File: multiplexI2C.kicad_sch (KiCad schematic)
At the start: 26 parts, among them J17 Conn_01x04_Pin, J18 PinSocket_1x20_P2.54mm_Vertic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, J19 PinSocket_1x20_P2.54mm_Vertic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, J20 Screw_Terminal_01x02, J9 header_0.25sqmm_1x04_P4.2mm_D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, U1 TCA9548A

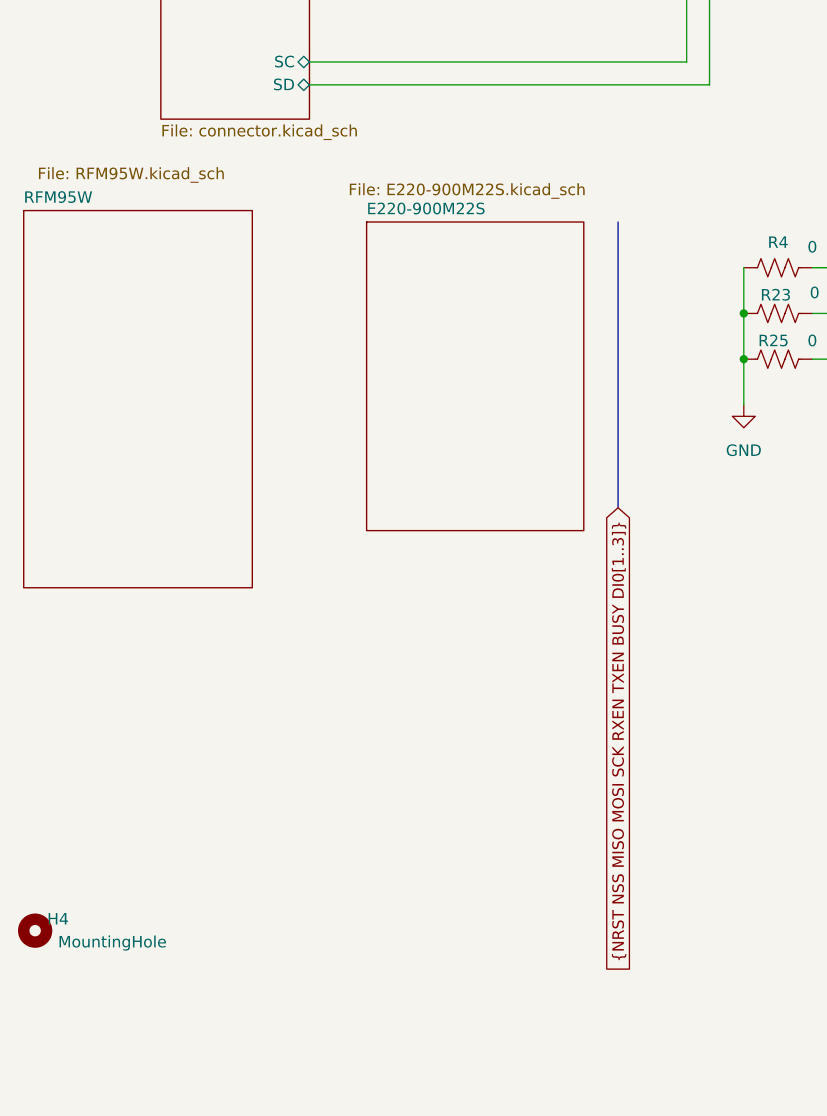
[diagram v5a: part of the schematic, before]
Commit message: DRC ot errors. 3D not showing U2.
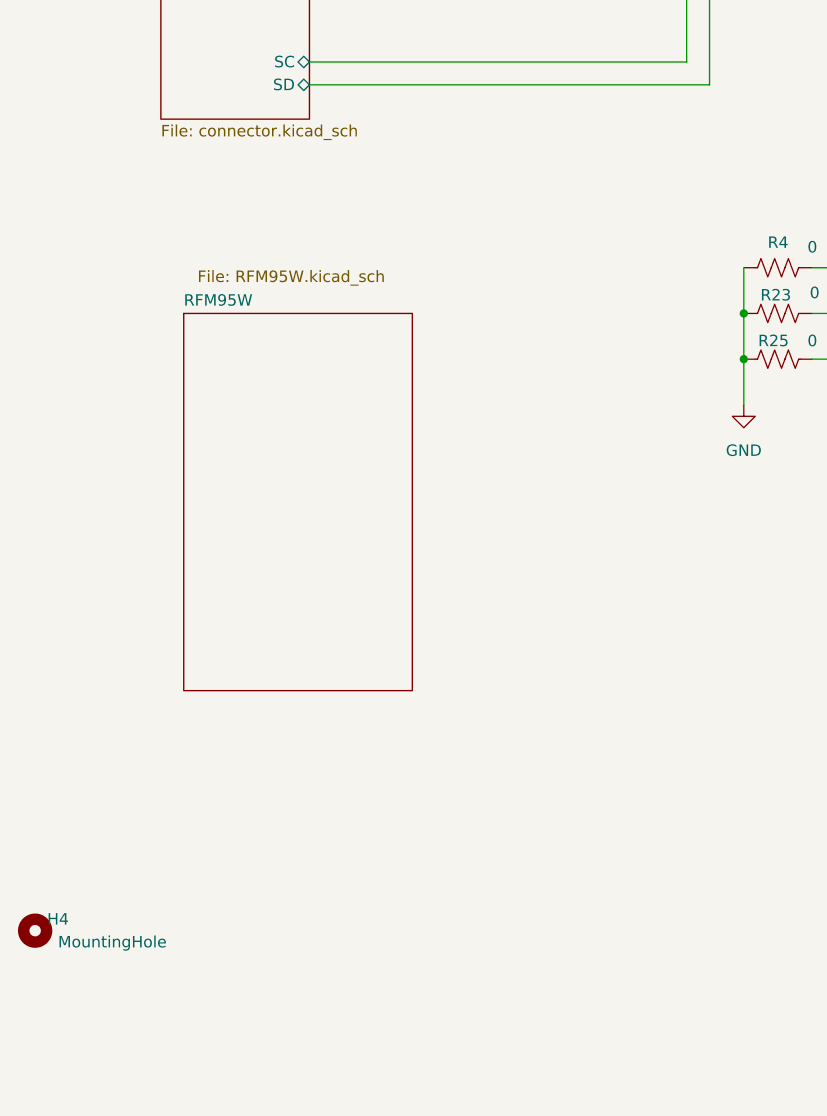
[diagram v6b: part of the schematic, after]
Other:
- removed sheet E220-900M22S
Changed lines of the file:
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@@
 		)
 	)
-	(bus
-		(pts
-			(xy 83.82 181.61) (xy 83.82 213.36)
-		)
-		(stroke
-			(width 0)
-			(type default)
-		)
-	)
 	(wire
 		(pts
@@
 		)
 	)
-	(global_label "{NRST NSS MISO MOSI SCK RXEN TXEN BUSY DI0[1..3]}"
-		(shape input)
-		(at 83.82 213.36 270)
-		(fields_autoplaced yes)
-		(effects
-			(font
-				(size 1.27 1.27)
-			)
-			(justify right)
-		)
-		(property "Intersheetrefs" "${INTERSHEET_REFS}"
-			(at 83.82 270.1689 90)
-			(effects
-				(font
-					(size 1.27 1.27)
-				)
-				(justify right)
-				(hide yes)
-			)
-		)
-	)
 	(global_label "{RESET NSS MISO MOSI SCK DIO0 DIO1}"
 		(shape bidirectional)
@@
 	)
 	(sheet
-		(at 17.78 180.34)
+		(at 35.56 191.77)
 		(size 25.4 41.91)
 		(stroke
@@
 		)
 		(property "Sheetname" "RFM95W"
-			(at 17.78 179.6284 0)
+			(at 35.56 191.0584 0)
 			(effects
 				(font
@@
 		)
 		(property "Sheetfile" "RFM95W.kicad_sch"
-			(at 19.304 175.514 0)
+			(at 37.084 186.944 0)
 			(effects
 				(font
@@
 				)
 			)
-		)
-	)
-	(sheet
-		(at 55.88 181.61)
-		(size 24.13 34.29)
-		(stroke
-			(width 0.1524)
-			(type solid)
-		)
-		(fill
-			(color 0 0 0 0.0000)
-		)
-		(property "Sheetname" "E220-900M22S"
-			(at 55.88 180.8984 0)
-			(effects
-				(font
-					(size 1.27 1.27)
-				)
-				(justify left bottom)
-			)
-		)
-		(property "Sheetfile" "E220-900M22S.kicad_sch"
-			(at 53.848 177.292 0)
-			(effects
-				(font
-					(size 1.27 1.27)
-				)
-				(justify left top)
-			)
-		)
-		(instances
-			(project "multiplexI2C"
-				(path "/0c2d0c14-8850-4a30-bb78-b2f40cb442ba"
-					(page "11")
-				)
-			)

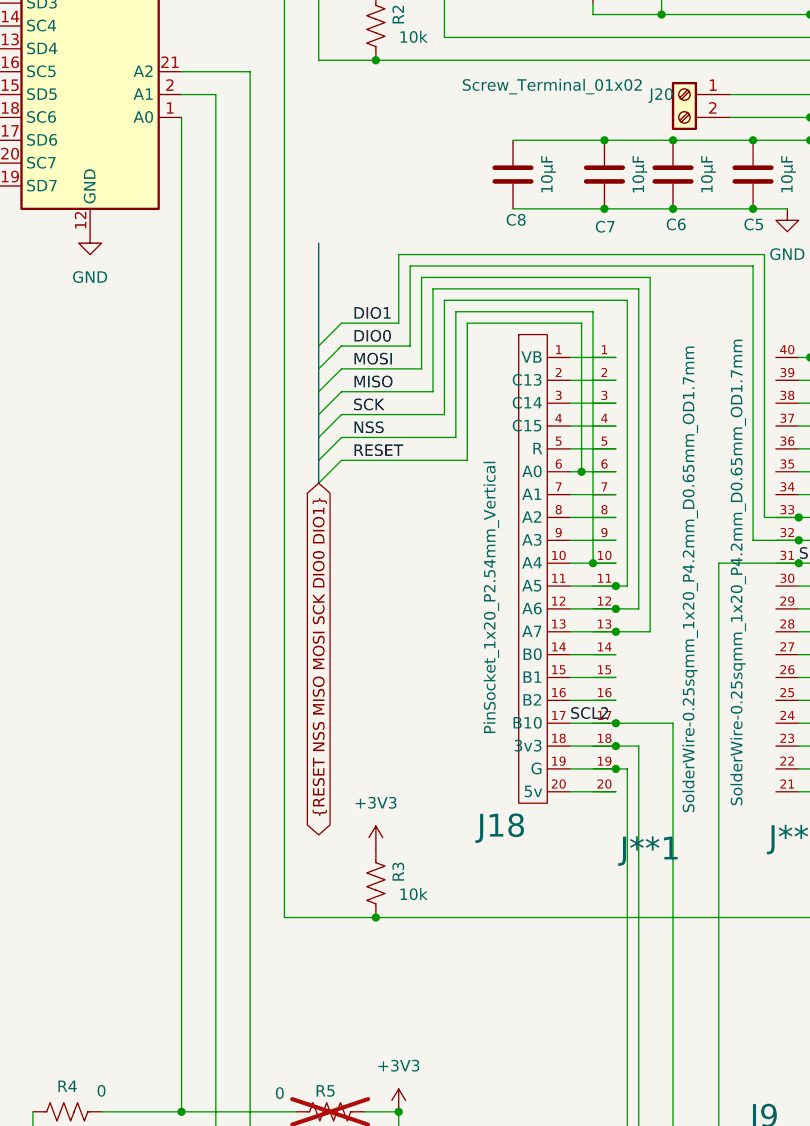
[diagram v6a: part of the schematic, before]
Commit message: added antenna connector.
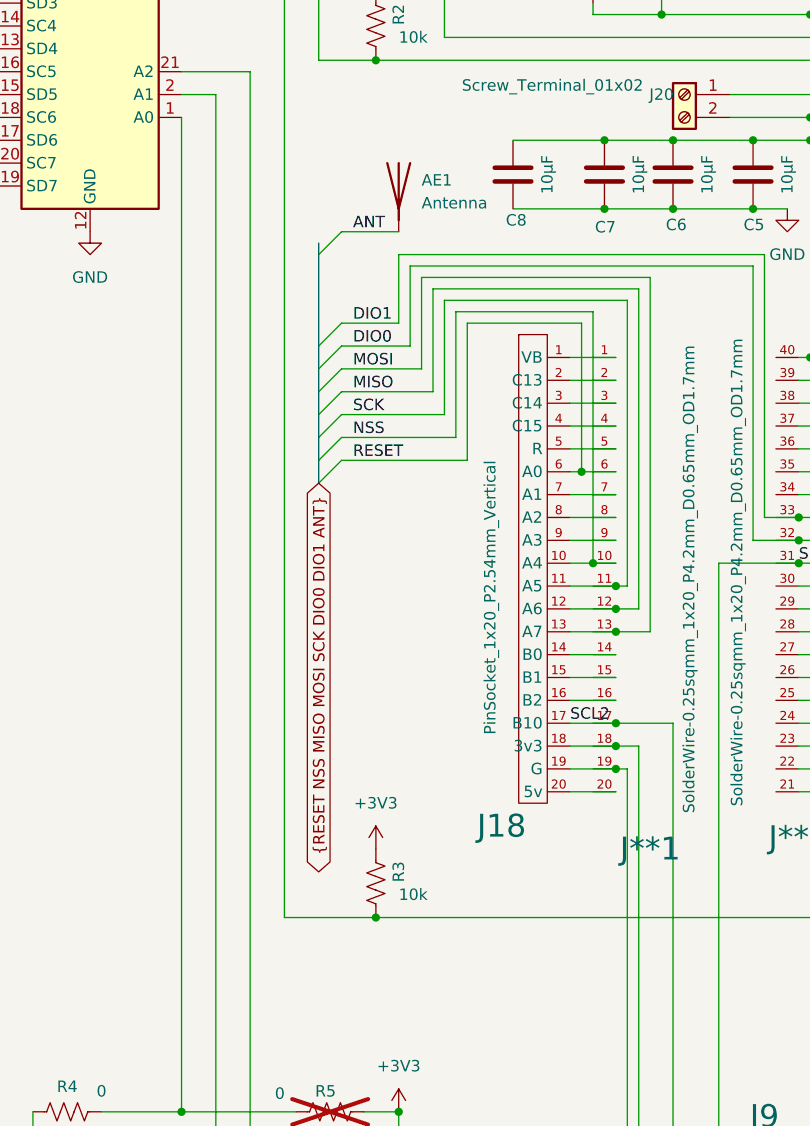
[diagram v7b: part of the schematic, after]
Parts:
- added AE1: Antenna, ProjectLib:PinSocket_1x01_P2.54mm_Horizontal, symbol Device:Antenna
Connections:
- new net ANT: AE1.1 (A)
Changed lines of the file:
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@@
 	)
 	(bus_entry
+		(at 129.54 91.44)
+		(size 2.54 -2.54)
+		(stroke
+			(width 0)
+			(type default)
+		)
+	)
+	(bus_entry
 		(at 129.54 106.68)
 		(size 2.54 -2.54)
@@
 	(wire
 		(pts
+			(xy 132.08 88.9) (xy 138.43 88.9)
+		)
+		(stroke
+			(width 0)
+			(type default)
+		)
+	)
+	(wire
+		(pts
 			(xy 157.48 133.35) (xy 162.56 133.35)
 		)
@@
 	(bus
 		(pts
-			(xy 129.54 90.17) (xy 129.54 101.6)
+			(xy 129.54 90.17) (xy 129.54 91.44)
 		)
 		(stroke
@@
 		)
 	)
+	(bus
+		(pts
+			(xy 129.54 91.44) (xy 129.54 101.6)
+		)
+		(stroke
+			(width 0)
+			(type default)
+		)
+	)
 	(wire
 		(pts
@@
 		)
 	)
-	(global_label "{RESET NSS MISO MOSI SCK DIO0 DIO1}"
+	(label "ANT"
+		(at 133.35 88.9 0)
+		(effects
+			(font
+				(size 1.27 1.27)
+			)
+			(justify left bottom)
+		)
+	)
+	(global_label "{RESET NSS MISO MOSI SCK DIO0 DIO1 ANT}"
 		(shape bidirectional)
 		(at 129.54 116.84 270)
@@
 		)
 		(property "Intersheetrefs" "${INTERSHEET_REFS}"
-			(at 129.54 159.7016 90)
+			(at 129.54 164.0559 90)
 			(effects
 				(font
@@
 					(unit 1)
 				)
+			)
+		)
+	)
+	(symbol
+		(lib_id "Device:Antenna")
+		(at 138.43 83.82 0)
+		(unit 1)
+		(exclude_from_sim no)
+		(in_bom yes)
+		(on_board yes)
+		(dnp no)
+		(fields_autoplaced yes)
+		(property "Reference" "AE1"
+			(at 140.97 83.1849 0)
+			(effects
+				(font
+					(size 1.27 1.27)
+				)
+				(justify left)
+			)
+		)
+		(property "Value" "Antenna"
+			(at 140.97 85.7249 0)
+			(effects
+				(font
+					(size 1.27 1.27)
+				)
+				(justify left)
+			)
+		)
+		(property "Footprint" "ProjectLib:PinSocket_1x01_P2.54mm_Horizontal"
+			(at 138.43 83.82 0)
+			(effects
+				(font
+					(size 1.27 1.27)
+				)
+				(hide yes)
+			)
+		)
+		(property "Datasheet" "~"
+			(at 138.43 83.82 0)
+			(effects
+				(font
+					(size 1.27 1.27)
+				)
+				(hide yes)
+			)
+		)
+		(property "Description" "Antenna"
+			(at 138.43 83.82 0)
+			(effects
+				(font
+					(size 1.27 1.27)
+				)
+				(hide yes)
+			)
+		)
+		(pin "1"
+		)
+		(instances
+			(project ""
+				(path "/0c2d0c14-8850-4a30-bb78-b2f40cb442ba"
+					(reference "AE1")
+					(unit 1)
+				)

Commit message: added antenna. No 3d yet.
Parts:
- AE1: footprint ProjectLib:PinSocket_1x01_P2.54mm_Horizontal -> ProjectLib:915MHz_spring_antenna
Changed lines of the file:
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@@
 	(label "DIO0"
 		(at 133.35 101.6 0)
+		(fields_autoplaced yes)
 		(effects
 			(font
@@
 	(label "DIO1"
 		(at 133.35 99.06 0)
+		(fields_autoplaced yes)
 		(effects
 			(font
@@
 	(label "RESET"
 		(at 133.35 114.3 0)
+		(fields_autoplaced yes)
 		(effects
 			(font
@@
 	(label "ANT"
 		(at 133.35 88.9 0)
+		(fields_autoplaced yes)
 		(effects
 			(font
@@
 			)
 		)
-		(property "Footprint" "ProjectLib:PinSocket_1x01_P2.54mm_Horizontal"
+		(property "Footprint" "ProjectLib:915MHz_spring_antenna"
 			(at 138.43 83.82 0)
 			(effects
@@
 			)
 		)
-		(property "Datasheet" "~"
+		(property "Datasheet" "https://www.nicerf.com/rf-antenna/915mhz-spring-antenna-sw915-th06.html"
 			(at 138.43 83.82 0)
 			(effects
